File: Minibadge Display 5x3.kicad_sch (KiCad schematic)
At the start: 3 parts, among them J1 Conn_01x08_Socket, U1 RP2040

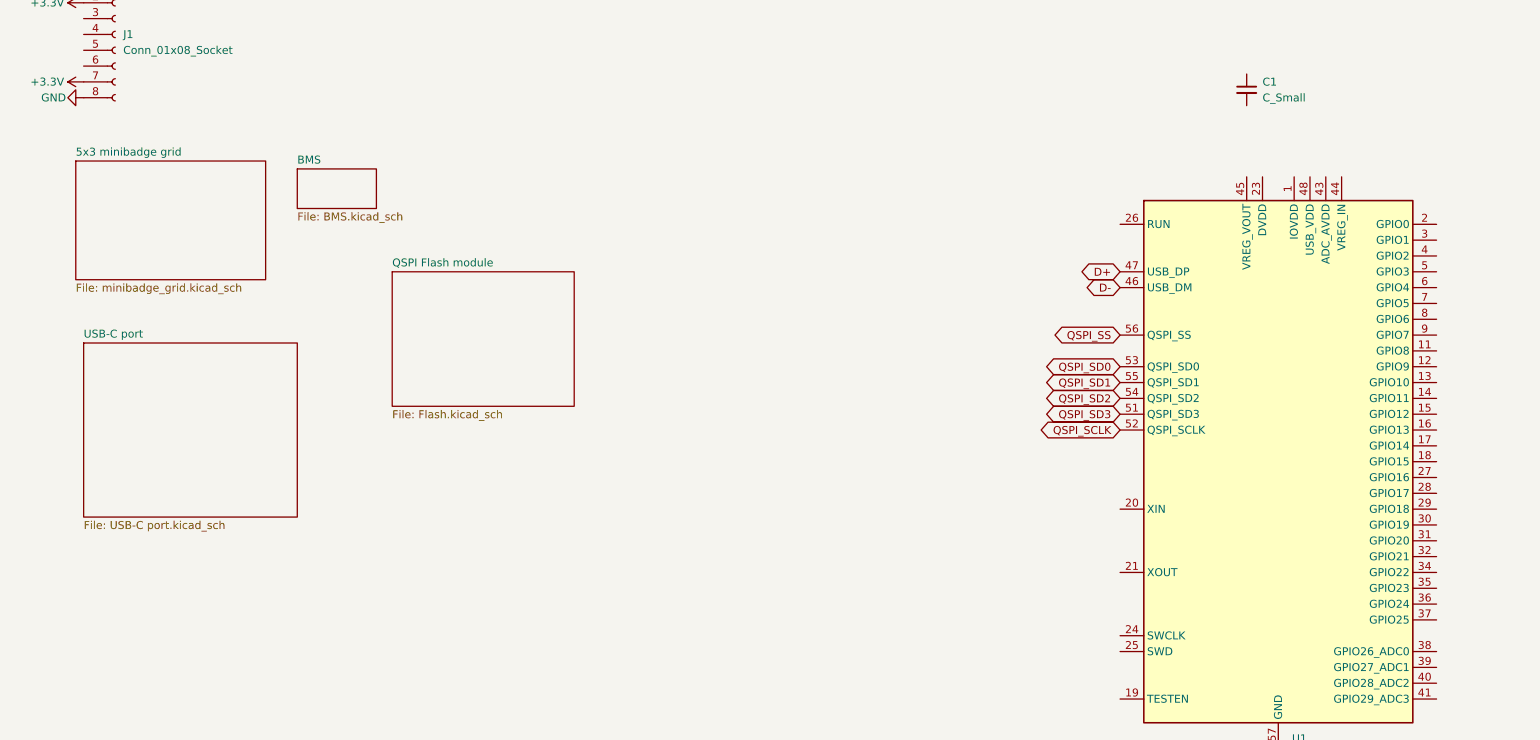
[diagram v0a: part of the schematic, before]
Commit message: flash + bms + usb switch
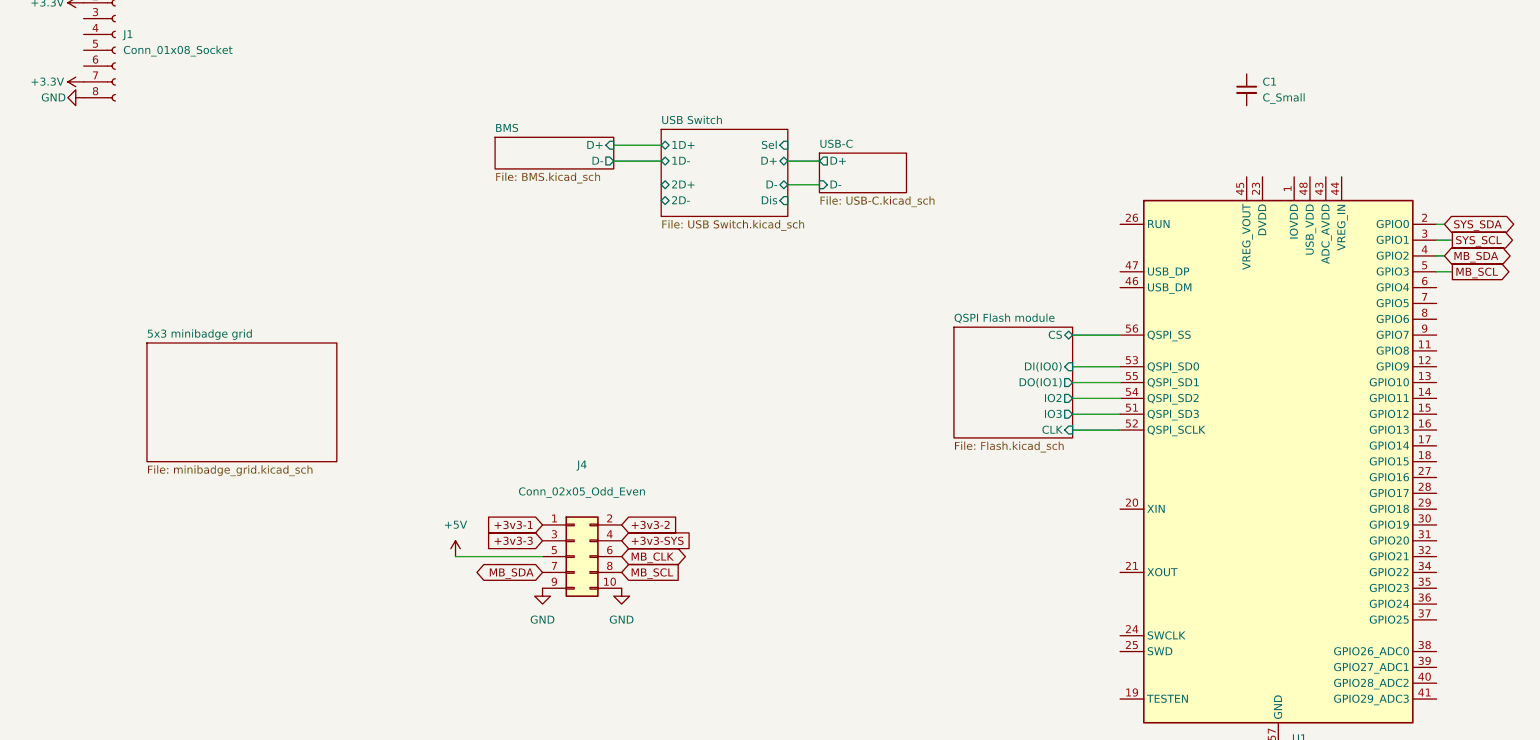
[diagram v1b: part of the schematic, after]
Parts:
- added J4: Conn_02x05_Odd_Even, symbol Connector_Generic:Conn_02x05_Odd_Even
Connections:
- net GND: now also J4.10 (Pin_10), J4.9 (Pin_9)
- net SYS_SDA: now reaches U1.2 (GPIO0)
- net SYS_SCL: now reaches U1.3 (GPIO1)
- net MB_SDA: now reaches U1.4 (GPIO2)
- net MB_SDA: now also J4.7 (Pin_7)
- net MB_SCL: now reaches U1.5 (GPIO3)
- net MB_SCL: now also J4.8 (Pin_8)
- net D+: no longer names the net of U1.47 (USB_DP)
- net D-: no longer names the net of U1.46 (USB_DM)
- net QSPI_SCLK renamed QSPI Flash module/CLK
- net QSPI_SD0 renamed QSPI Flash module/DI(IO0)
- net QSPI_SD1 renamed QSPI Flash module/DO(IO1)
- net QSPI_SD2 renamed QSPI Flash module/IO2
- net QSPI_SD3 renamed QSPI Flash module/IO3
- net QSPI_SS renamed QSPI Flash module/CS
- new net +3v3-1: J4.1 (Pin_1)
- new net +3v3-2: J4.2 (Pin_2)
- new net +3v3-3: J4.3 (Pin_3)
- new net +3v3-SYS: J4.4 (Pin_4)
- new net +5V: J4.5 (Pin_5)
- new net MB_CLK: J4.6 (Pin_6)
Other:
- sheet USB-C port renamed USB-C
- added sheet USB Switch (USB Switch.kicad_sch)
- sheet BMS ports: added D+, D-; removed none
- sheet QSPI Flash module ports: added CLK, CS, DI(IO0), DO(IO1), IO2, IO3; removed none
- sheet USB-C: file USB-C port.kicad_sch -> USB-C.kicad_sch
- sheet USB-C ports: added D+, D-; removed none

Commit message: BMS work
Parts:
- removed J1: Conn_01x08_Socket, Connector_PinHeader_2.54mm:PinHeader_1x08_P2.54mm_Horizontal, symbol Connector:Conn_01x08_Socket
- removed U1: RP2040, Package_DFN_QFN:QFN-56-1EP_7x7mm_P0.4mm_EP3.2x3.2mm, symbol MCU_RaspberryPi:RP2040
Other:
- added sheet RP2040 (RP2040.kicad_sch)
- sheet BMS ports: added DSEL; removed none
- note removed: "Lighting control I2C System bus access for BMS single button that serves as power on/off + lighting control"

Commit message: more rp2040 work
-BMS updates
- rp2040 updates
- add hardware design docs
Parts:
- removed C1: C_Small, symbol Device:C_Small
- J4: value Conn_02x05_Odd_Even -> Board to Board
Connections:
- net +3v3-SYS renamed +VBATT
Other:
- sheet USB-C renamed USB-C Port
- sheet BMS ports: added CE, INT, OTG, SCL, SDA; removed none
- sheet RP2040 ports: added QSPI_SCLK, QSPI_SD0, QSPI_SD1, QSPI_SD2, QSPI_SD3, QSPI_SS, SCL1, SCL2, SDA1, SDA2; removed none

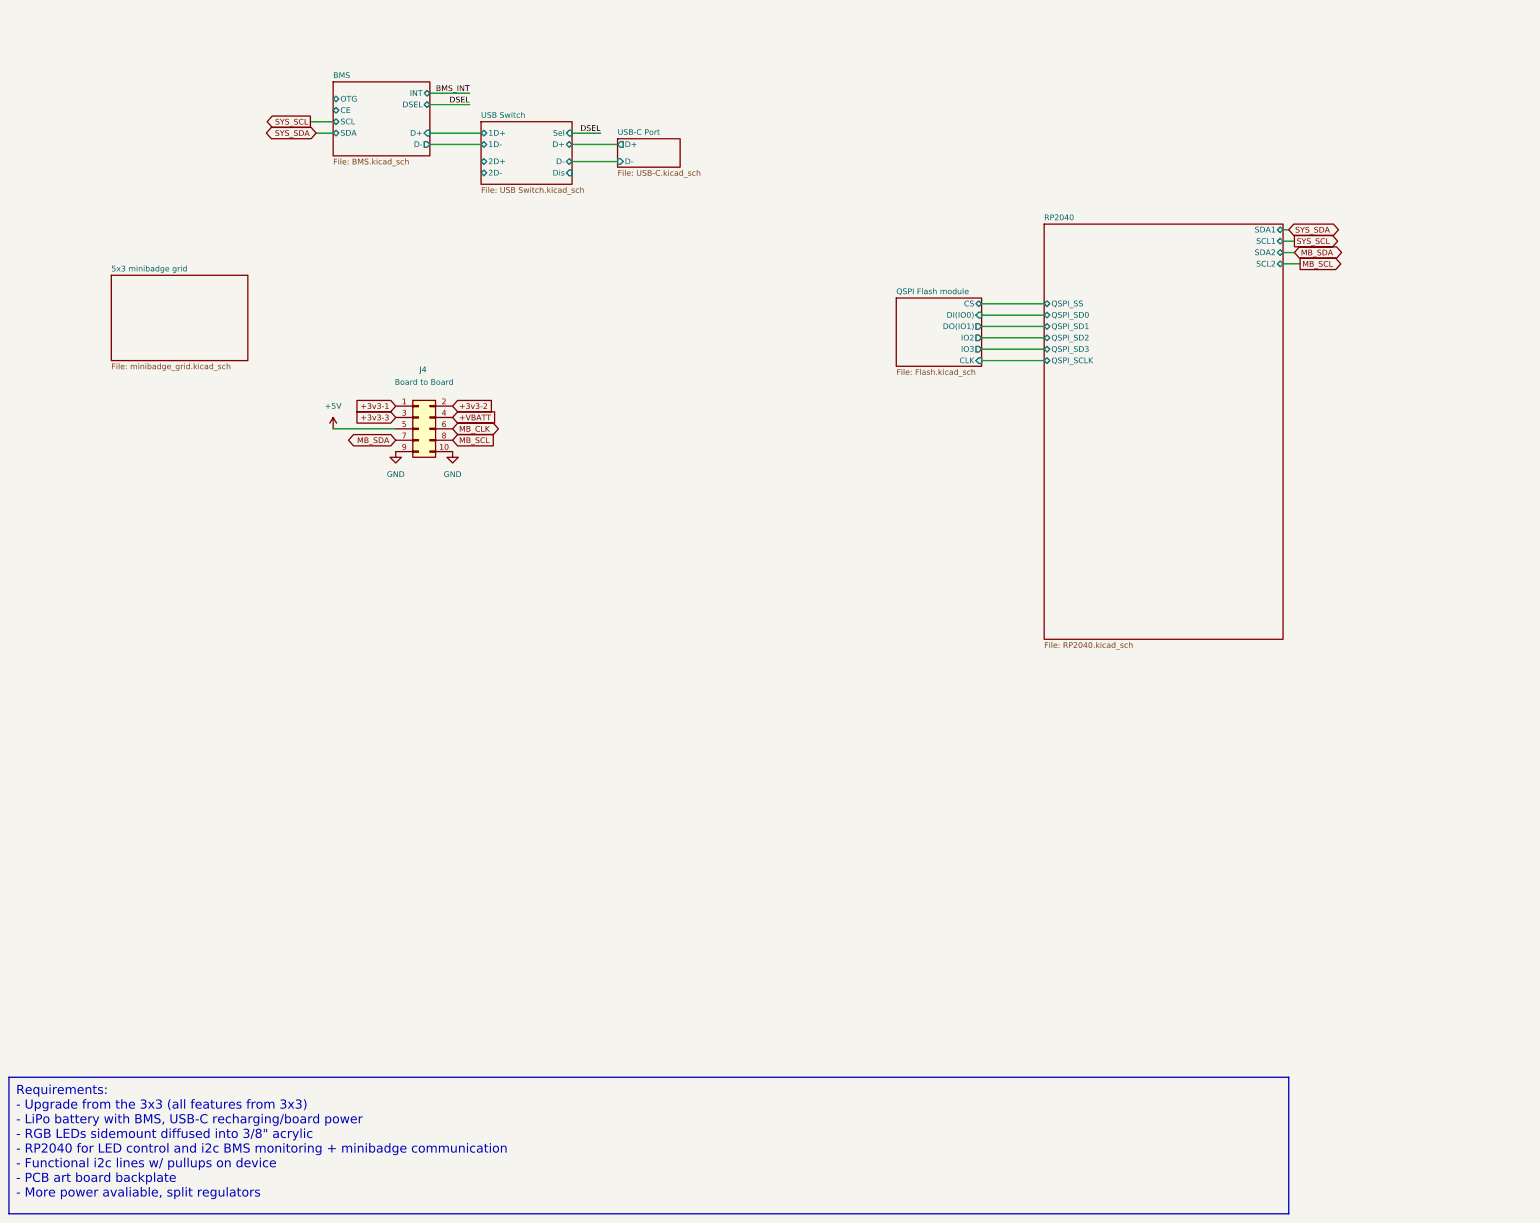
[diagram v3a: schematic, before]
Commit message: BMS updates
- BMS mostly done
- all BMS pins connected to RP2040
- Re-did Minibadge pinouts
- Connected RP2040 to USB Switch
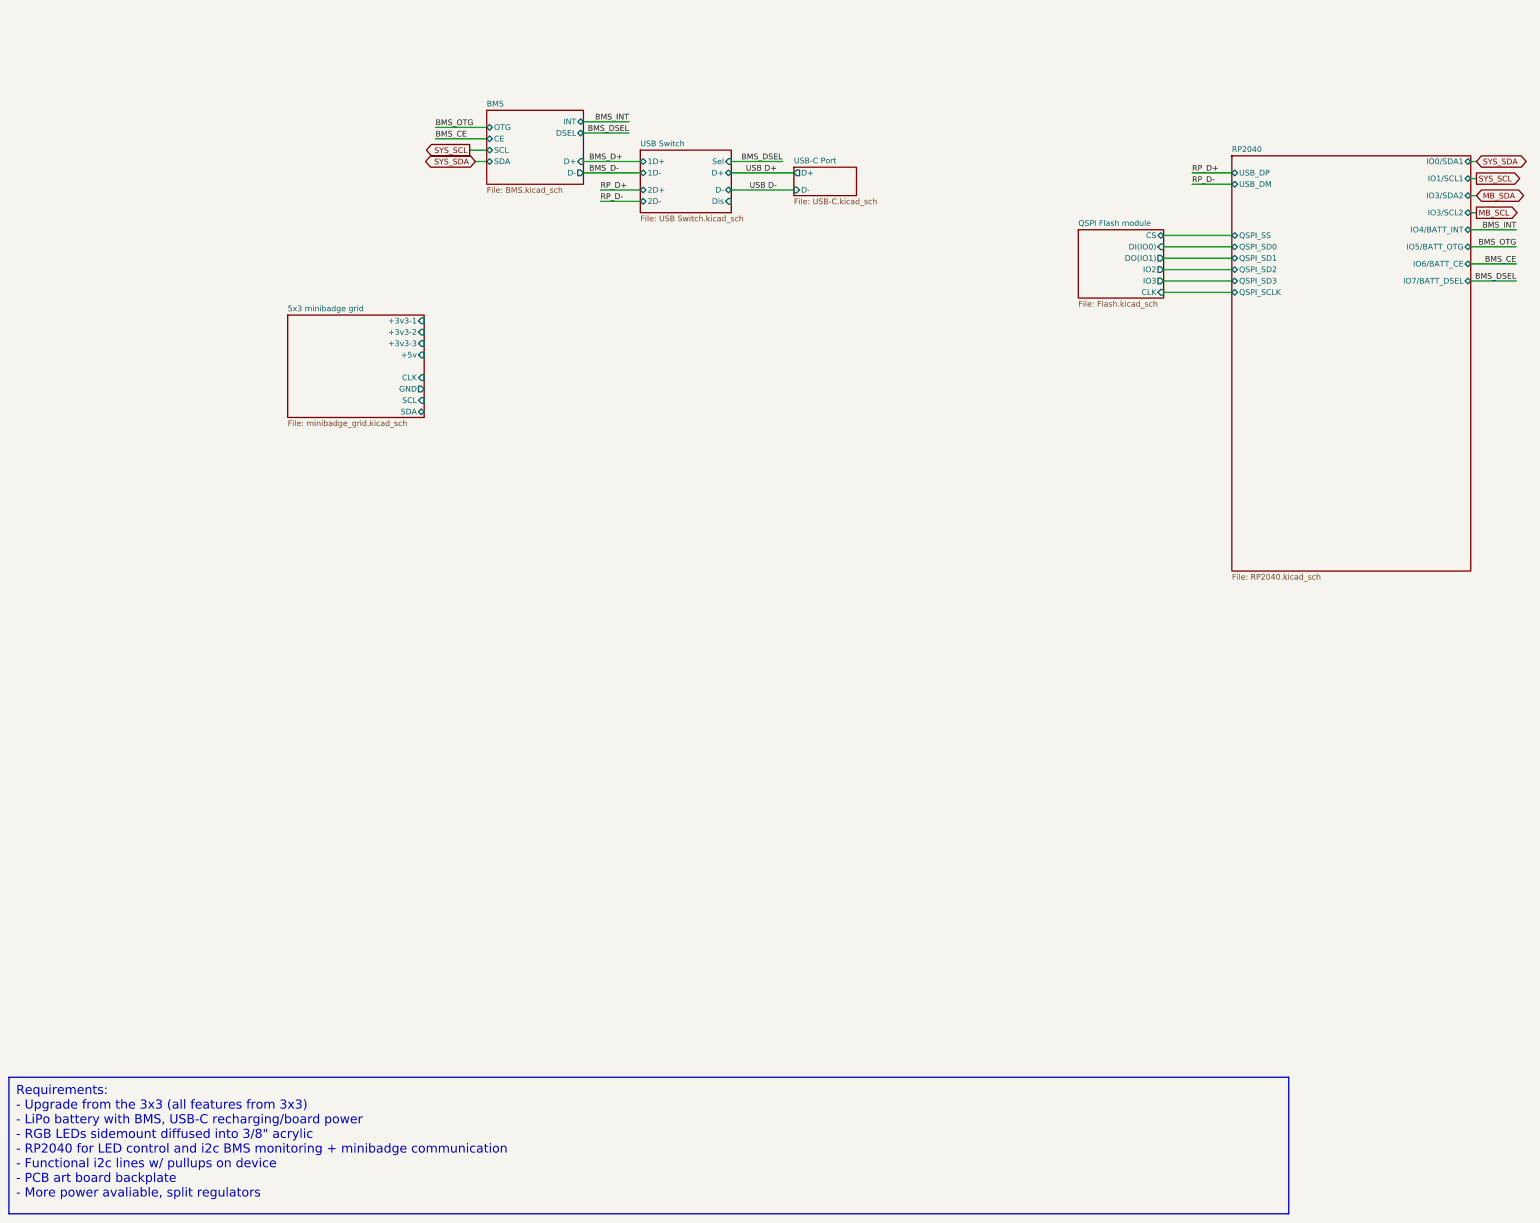
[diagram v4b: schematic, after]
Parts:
- removed J4: Board to Board, symbol Connector_Generic:Conn_02x05_Odd_Even
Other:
- sheet 5x3 minibadge grid ports: added +3v3-1, +3v3-2, +3v3-3, +5v, CLK, GND, SCL, SDA; removed none
- sheet RP2040 ports: added IO0/SDA1, IO1/SCL1, IO3/SCL2, IO3/SDA2, IO4/BATT_INT, IO5/BATT_OTG, IO6/BATT_CE, IO7/BATT_DSEL, USB_DM, USB_DP; removed SCL1, SCL2, SDA1, SDA2

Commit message: cleanup
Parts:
- added J1: Board to Board, symbol Connector_Generic:Conn_02x05_Odd_Even
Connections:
- net MB_SCL: now also J1.8 (Pin_8)
- net MB_SDA: now also J1.7 (Pin_7)
- new net +3v3-1: J1.1 (Pin_1)
- new net +3v3-2: J1.2 (Pin_2)
- new net +3v3-3: J1.3 (Pin_3)
- new net +5V: J1.5 (Pin_5)
- new net +VBATT: J1.4 (Pin_4)
- new net GND: J1.10 (Pin_10), J1.9 (Pin_9)
- new net MB_CLK: J1.6 (Pin_6)
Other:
- sheet RP2040 ports: added IO7/USB_SW_DSEL, IO8/USB_SW_DISABLE; removed IO7/BATT_DSEL
